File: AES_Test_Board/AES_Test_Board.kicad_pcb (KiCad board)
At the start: 2 copper layers, 65 x 65 mm, 38 parts, among them J1 Conn_02x06_Top_Bottom, J2 Conn_02x06_Top_Bottom, J3 Conn_01x02_Pin, U3 TCR3RM10A

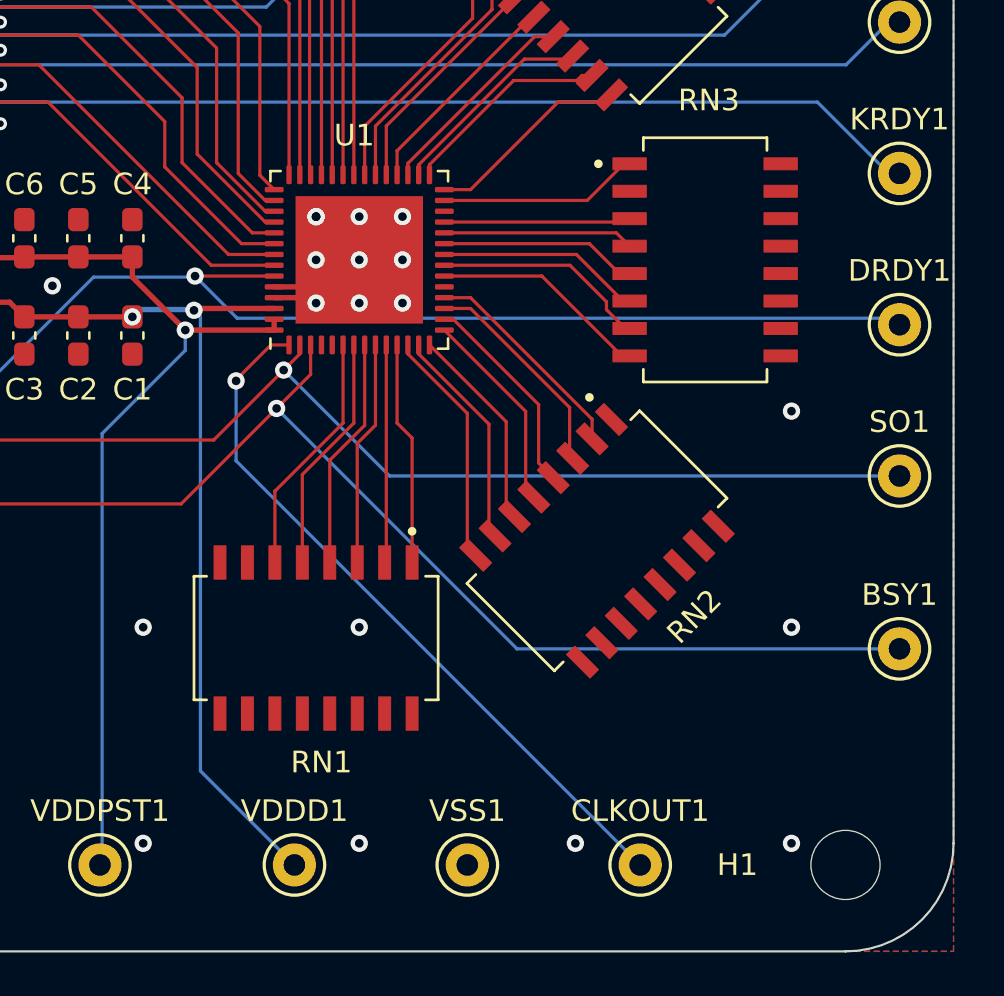
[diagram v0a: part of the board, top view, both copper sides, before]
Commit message: Added power pins to connection
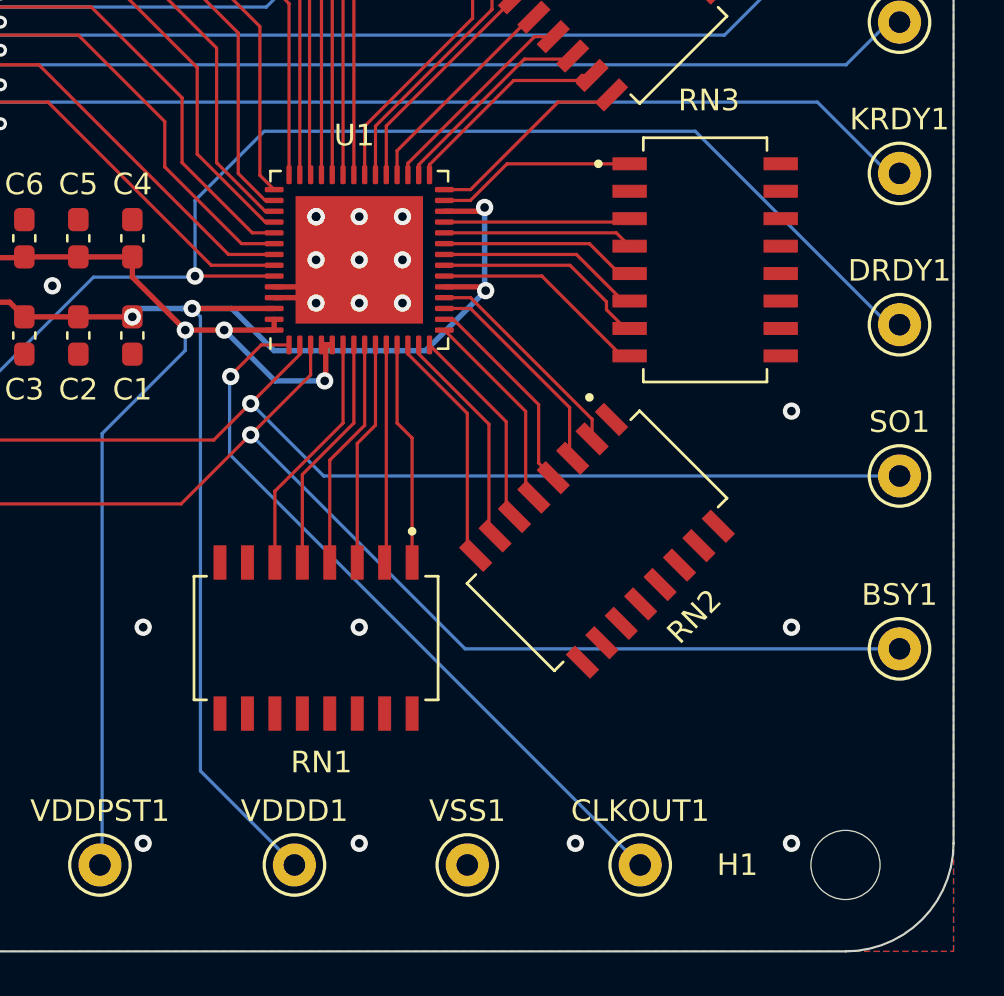
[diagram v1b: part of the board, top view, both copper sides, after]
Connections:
- U1 pad 19: unconnected-(U1-MLPINS-Pad19) -> /VDDD
- U1 pad 26: unconnected-(U1-MLPINS-Pad26) -> /VDDD
- U1 pad 4: unconnected-(U1-MLPINS-Pad4) -> /VDDPST
- U1 pad 5: unconnected-(U1-MLPINS-Pad5) -> /VDDPST
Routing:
- net /VDDD: track 43.1 -> 67.0 mm, vias 2 -> 4
- net /VDDPST: track 63.8 -> 71.9 mm, vias 1 -> 3
- net /DRDY: track 64.3 -> 71.9 mm
- net /SCAN_OUT: track 62.9 -> 63.8 mm
- net /BSY: track 68.0 -> 68.7 mm
- net /CLKOUT: track 33.3 -> 33.8 mm

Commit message: works nowA
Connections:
- RN1 pad 6: /MLPIN6 -> unconnected-(RN1-Pad6)
- RN3 pad 7: /MLPIN21 -> unconnected-(RN3-Pad7)
- RN4 pad 8: /MLPIN28 -> unconnected-(RN4-Pad8)
- U1 pad 21: /MLPIN21 -> /VSS
- U1 pad 28: /MLPIN28 -> /VSS
- U1 pad 6: /MLPIN6 -> /VSS
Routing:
- net /MLPIN6: track 11.4 -> 0.00 mm
- net /MLPIN21: track 10.00 -> 0.00 mm
- net /MLPIN28: track 9.55 -> 0.00 mm
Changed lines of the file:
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@@
   (net 25 "unconnected-(RN1-Pad7)")
   (net 26 "unconnected-(RN1-Pad8)")
-  (net 27 "/MLPIN6")
+  (net 27 "unconnected-(RN1-Pad6)")
   (net 28 "/MLPIN7")
   (net 29 "/MLPIN8")
@@
   (net 40 "unconnected-(RN2-Pad1)")
   (net 41 "/MLPIN20")
-  (net 42 "/MLPIN21")
+  (net 42 "unconnected-(RN3-Pad7)")
   (net 43 "/MLPIN22")
   (net 44 "/MLPIN23")
@@
   (net 47 "unconnected-(RN3-Pad2)")
   (net 48 "/MLPIN27")
-  (net 49 "/MLPIN28")
+  (net 49 "unconnected-(RN4-Pad8)")
   (net 50 "/MLPIN29")
   (net 51 "/MLPIN30")
@@
       (net 50 "/MLPIN29") (pintype "passive") (solder_mask_margin 0.102))
     (pad "8" smd roundrect (at -3.495 4.445 45) (size 1.59 0.6) (layers "F.Cu" "F.Paste" "F.Mask") (roundrect_rratio 0.04)
-      (net 49 "/MLPIN28") (pintype "passive") (solder_mask_margin 0.102))
+      (net 49 "unconnected-(RN4-Pad8)") (pintype "passive+no_connect") (solder_mask_margin 0.102))
     (pad "9" smd roundrect (at 3.495 4.445 225) (size 1.59 0.6) (layers "F.Cu" "F.Paste" "F.Mask") (roundrect_rratio 0.04)
       (net 5 "/VSS") (pintype "passive") (solder_mask_margin 0.102))
@@
       (net 22 "/VDDPST") (pinfunction "VDDPST") (pintype "power_in"))
     (pad "6" smd roundrect (at -3.9375 -0.75 90) (size 0.875 0.25) (layers "F.Cu" "F.Paste" "F.Mask") (roundrect_rratio 0.25)
-      (net 27 "/MLPIN6") (pinfunction "MLPINS") (pintype "input"))
+      (net 5 "/VSS") (pinfunction "VSSPST") (pintype "power_in"))
     (pad "7" smd roundrect (at -3.9375 -0.25 90) (size 0.875 0.25) (layers "F.Cu" "F.Paste" "F.Mask") (roundrect_rratio 0.25)
       (net 28 "/MLPIN7") (pinfunction "MLPINS") (pintype "input"))
@@
       (net 41 "/MLPIN20") (pinfunction "MLPINS") (pintype "input"))
     (pad "21" smd roundrect (at -0.25 3.9375 90) (size 0.25 0.875) (layers "F.Cu" "F.Paste" "F.Mask") (roundrect_rratio 0.25)
-      (net 42 "/MLPIN21") (pinfunction "MLPINS") (pintype "input"))
+      (net 5 "/VSS") (pinfunction "VSS0") (pintype "power_in"))
     (pad "22" smd roundrect (at 0.25 3.9375 90) (size 0.25 0.875) (layers "F.Cu" "F.Paste" "F.Mask") (roundrect_rratio 0.25)
       (net 43 "/MLPIN22") (pinfunction "MLPINS") (pintype "input"))
@@
       (net 48 "/MLPIN27") (pinfunction "MLPINS") (pintype "input"))
     (pad "28" smd roundrect (at 3.25 3.9375 90) (size 0.25 0.875) (layers "F.Cu" "F.Paste" "F.Mask") (roundrect_rratio 0.25)
-      (net 49 "/MLPIN28") (pinfunction "MLPINS") (pintype "input"))
+      (net 5 "/VSS") (pinfunction "VSS0") (pintype "power_in"))
     (pad "29" smd roundrect (at 3.9375 3.25 90) (size 0.875 0.25) (layers "F.Cu" "F.Paste" "F.Mask") (roundrect_rratio 0.25)
       (net 50 "/MLPIN29") (pinfunction "MLPINS") (pintype "input"))
@@
       (net 43 "/MLPIN22") (pintype "passive") (solder_mask_margin 0.102))
     (pad "7" smd roundrect (at -3.495 3.175) (size 1.59 0.6) (layers "F.Cu" "F.Paste" "F.Mask") (roundrect_rratio 0.04)
-      (net 42 "/MLPIN21") (pintype "passive") (solder_mask_margin 0.102))
+      (net 42 "unconnected-(RN3-Pad7)") (pintype "passive+no_connect") (solder_mask_margin 0.102))
     (pad "8" smd roundrect (at -3.495 4.445) (size 1.59 0.6) (layers "F.Cu" "F.Paste" "F.Mask") (roundrect_rratio 0.04)
       (net 41 "/MLPIN20") (pintype "passive") (solder_mask_margin 0.102))
@@
       (net 28 "/MLPIN7") (pintype "passive") (solder_mask_margin 0.102))
     (pad "6" smd roundrect (at -3.495 1.905 270) (size 1.59 0.6) (layers "F.Cu" "F.Paste" "F.Mask") (roundrect_rratio 0.04)
-      (net 27 "/MLPIN6") (pintype "passive") (solder_mask_margin 0.102))
+      (net 27 "unconnected-(RN1-Pad6)") (pintype "passive+no_connect") (solder_mask_margin 0.102))
     (pad "7" smd roundrect (at -3.495 3.175 270) (size 1.59 0.6) (layers "F.Cu" "F.Paste" "F.Mask") (roundrect_rratio 0.04)
       (net 25 "unconnected-(RN1-Pad7)") (pintype "passive+no_connect") (solder_mask_margin 0.102))
@@
   (segment (start 111.8 90.25) (end 114.1 90.25) (width 0.25) (layer "B.Cu") (net 24))
   (segment (start 114.1 90.25) (end 116.05 92.2) (width 0.25) (layer "B.Cu") (net 24))
-  (segment (start 116.095 98.705) (end 116.095 102.005) (width 0.15) (layer "F.Cu") (net 27))
-  (segment (start 119.25 95.55) (end 116.095 98.705) (width 0.15) (layer "F.Cu") (net 27))
-  (segment (start 119.25 91.9375) (end 119.25 95.55) (width 0.15) (layer "F.Cu") (net 27))
   (segment (start 117.365 97.935) (end 117.365 102.005) (width 0.15) (layer "F.Cu") (net 28))
   (segment (start 119.75 95.55) (end 117.365 97.935) (width 0.15) (layer "F.Cu") (net 28))
@@
   (segment (start 132.145 92.445) (end 132.51 92.445) (width 0.15) (layer "F.Cu") (net 41))
   (segment (start 128.45 88.75) (end 132.145 92.445) (width 0.15) (layer "F.Cu") (net 41))
-  (segment (start 131.44 90.30485) (end 132.31015 91.175) (width 0.15) (layer "F.Cu") (net 42))
-  (segment (start 129.75 88.25) (end 131.44 89.94) (width 0.15) (layer "F.Cu") (net 42))
   (segment (start 132.31015 91.175) (end 132.51 91.175) (width 0.15) (layer "F.Cu") (net 42))
-  (segment (start 131.44 89.94) (end 131.44 90.30485) (width 0.15) (layer "F.Cu") (net 42))
-  (segment (start 123.9375 88.25) (end 129.75 88.25) (width 0.15) (layer "F.Cu") (net 42))
   (segment (start 130.05 87.75) (end 132.205 89.905) (width 0.15) (layer "F.Cu") (net 43))
   (segment (start 123.9375 87.75) (end 130.05 87.75) (width 0.15) (layer "F.Cu") (net 43))
@@
   (segment (start 125.144974 85.25) (end 126.839974 83.555) (width 0.15) (layer "F.Cu") (net 48))
   (segment (start 123.9375 85.25) (end 125.144974 85.25) (width 0.15) (layer "F.Cu") (net 48))
-  (segment (start 125.15 84.75) (end 123.9375 84.75) (width 0.15) (layer "F.Cu") (net 49))
-  (segment (start 129.2 80.7) (end 125.15 84.75) (width 0.15) (layer "F.Cu") (net 49))
-  (segment (start 131.336179 80.7) (end 129.2 80.7) (width 0.15) (layer "F.Cu") (net 49))
   (segment (start 131.671751 80.364428) (end 131.336179 80.7) (width 0.15) (layer "F.Cu") (net 49))
   (segment (start 130.070064 79.7) (end 127.143826 79.7) (width 0.15) (layer "F.Cu") (net 50))
